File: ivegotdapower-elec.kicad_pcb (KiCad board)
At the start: 2 copper layers, 100 x 50 mm, 0 parts

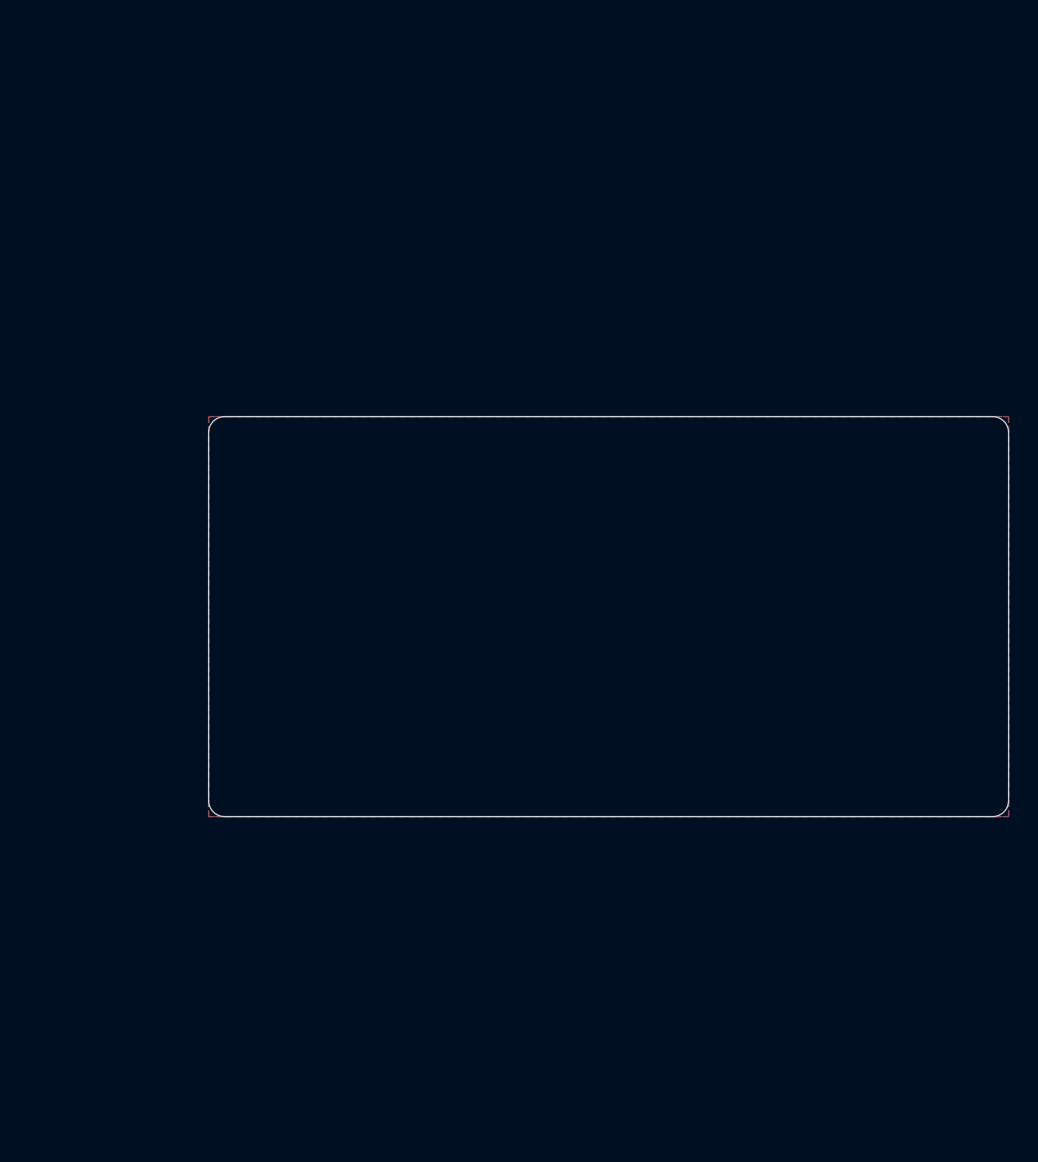
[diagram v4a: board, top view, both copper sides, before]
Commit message: power routed
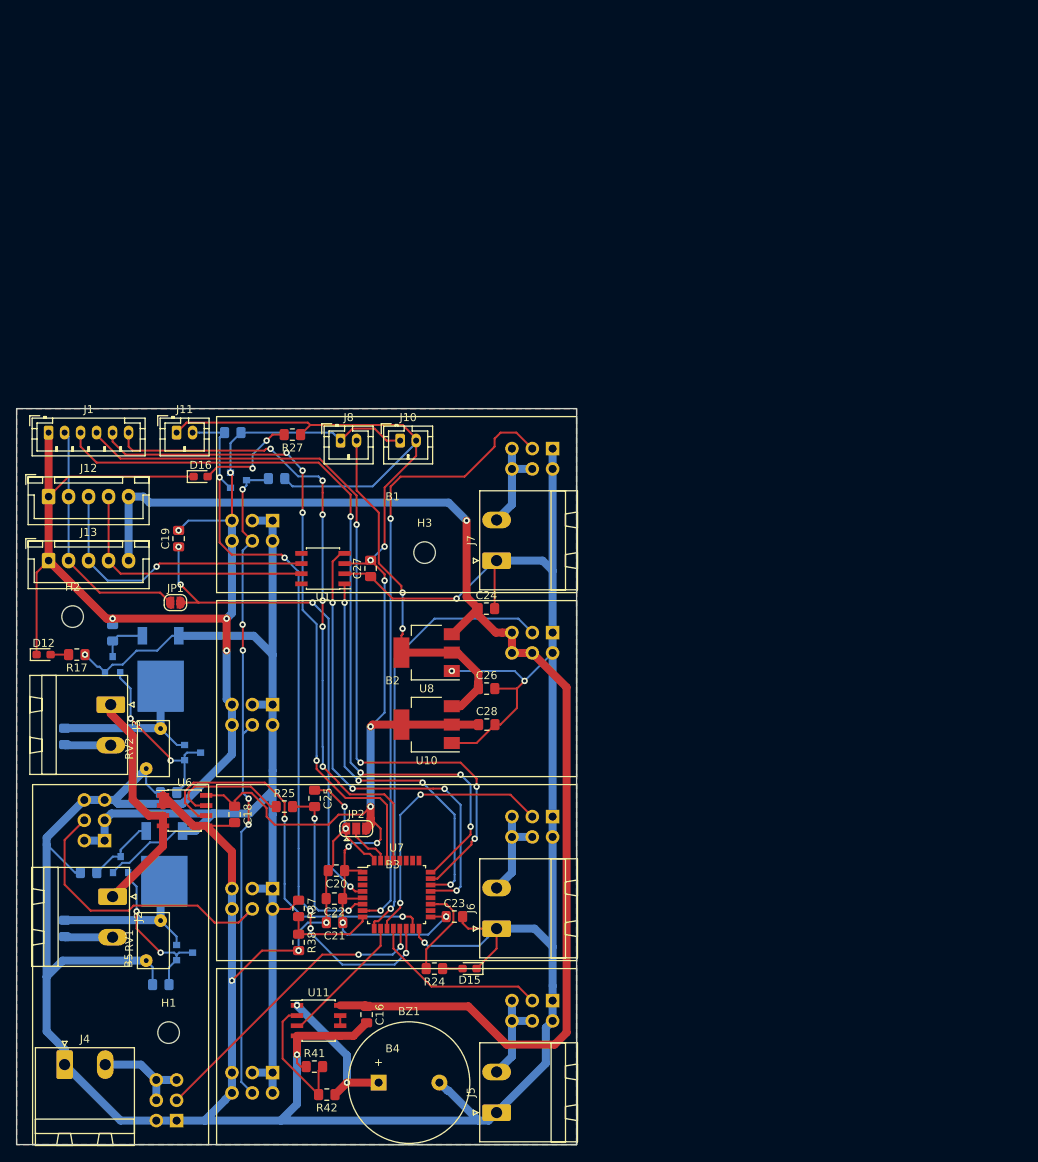
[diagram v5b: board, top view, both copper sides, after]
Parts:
- added B1: board_fille, board_fille:board_fille, F.Cu at (123.0, 110.0)
- added B2: board_fille, board_fille:board_fille, F.Cu at (123.0, 133.0)
- added B3: board_fille, board_fille:board_fille, F.Cu at (123.0, 156.0)
- added B4: board_fille, board_fille:board_fille, F.Cu at (123.0, 179.0)
- added B5: board_fille, board_fille:board_fille, F.Cu at (90.0, 168.0)
- added BZ1: Buzzer, Buzzer_Beeper:Buzzer_15x7.5RM7.6, F.Cu at (121.2, 183.2)
- added C16: C, Capacitor_SMD:C_0805_2012Metric_Pad1.15x1.40mm_HandSolder, F.Cu at (119.8, 174.8)
- added C18: 100nF, Capacitor_SMD:C_0805_2012Metric_Pad1.15x1.40mm_HandSolder, F.Cu at (103.2, 149.7)
- added C19: 100nF, Capacitor_SMD:C_0805_2012Metric_Pad1.15x1.40mm_HandSolder, F.Cu at (96.2, 115.2)
- added C20: 100nF, Capacitor_SMD:C_0805_2012Metric_Pad1.15x1.40mm_HandSolder, F.Cu at (116.0, 156.8)
- added C21: 100nF, Capacitor_SMD:C_0805_2012Metric_Pad1.15x1.40mm_HandSolder, F.Cu at (115.8, 163.2)
- added C22: 4.7uF, Capacitor_SMD:C_0805_2012Metric_Pad1.15x1.40mm_HandSolder, F.Cu at (115.7, 160.2)
- added C23: 100nF, Capacitor_SMD:C_0805_2012Metric_Pad1.15x1.40mm_HandSolder, F.Cu at (130.7, 162.5)
- added C24: 100nF, Capacitor_SMD:C_0805_2012Metric_Pad1.15x1.40mm_HandSolder, F.Cu at (134.7, 124.0)
- added C25: C, Capacitor_SMD:C_0805_2012Metric_Pad1.15x1.40mm_HandSolder, F.Cu at (113.2, 147.7)
- added C26: C, Capacitor_SMD:C_0805_2012Metric_Pad1.15x1.40mm_HandSolder, F.Cu at (134.8, 134.0)
- added C27: 100nF, Capacitor_SMD:C_0805_2012Metric_Pad1.15x1.40mm_HandSolder, F.Cu at (120.2, 119.0)
- added C28: 10uF, Capacitor_SMD:C_0805_2012Metric_Pad1.15x1.40mm_HandSolder, F.Cu at (134.8, 138.5)
- added D12: LED, LED_SMD:LED_0603_1608Metric_Pad1.05x0.95mm_HandSolder, F.Cu at (79.4, 129.8)
- added D15: LED, LED_SMD:LED_0603_1608Metric_Pad1.05x0.95mm_HandSolder, F.Cu at (132.6, 169.0)
- added D16: LED, LED_SMD:LED_0603_1608Metric_Pad1.05x0.95mm_HandSolder, F.Cu at (99.0, 107.5)
- added F6: Fuse, Fuse:Fuse_0805_2012Metric_Pad1.15x1.40mm_HandSolder, B.Cu at (82.0, 164.0)
- added F7: Fuse, Fuse:Fuse_0805_2012Metric_Pad1.15x1.40mm_HandSolder, B.Cu at (82.0, 140.0)
- added H1: MountingHole, MountingHole:MountingHole_2.7mm_M2.5, F.Cu at (95.0, 177.0)
- added H2: MountingHole, MountingHole:MountingHole_2.7mm_M2.5, F.Cu at (83.0, 125.0)
- added H3: MountingHole, MountingHole:MountingHole_2.7mm_M2.5, F.Cu at (127.0, 117.0)
- added J1: Conn_Debug, Connector_JST:JST_PH_B6B-PH-K_1x06_P2.00mm_Vertical, F.Cu at (80.0, 102.0)
- added J10: Conn_+3.3V, Connector_JST:JST_PH_B2B-PH-K_1x02_P2.00mm_Vertical, F.Cu at (123.9, 103.0)
- added J11: Conn_bau, Connector_JST:JST_PH_B2B-PH-K_1x02_P2.00mm_Vertical, F.Cu at (96.0, 102.0)
- added J12: CAN_conn, Connector_JST:JST_XH_B05B-XH-A_1x05_P2.50mm_Vertical, F.Cu at (80.0, 110.0)
- added J13: CAN_conn, Connector_JST:JST_XH_B05B-XH-A_1x05_P2.50mm_Vertical, F.Cu at (80.0, 118.0)
- added J2: Conn_batt, Connector_Phoenix_MSTB:PhoenixContact_MSTBA_2,5_2-G-5,08_1x02_P5.08mm_Horizontal, F.Cu at (88.0, 160.0)
- added J3: Conn_alim, Connector_Phoenix_MSTB:PhoenixContact_MSTBA_2,5_2-G-5,08_1x02_P5.08mm_Horizontal, F.Cu at (87.8, 136.0)
- added J4: Conn_TSMR, Connector_Phoenix_MSTB:PhoenixContact_MSTBA_2,5_2-G-5,08_1x02_P5.08mm_Horizontal, F.Cu at (82.0, 181.0)
- added J5: Conn_POW2, Connector_Phoenix_MSTB:PhoenixContact_MSTBA_2,5_2-G-5,08_1x02_P5.08mm_Horizontal, F.Cu at (136.0, 187.0)
- added J6: Conn_POW1, Connector_Phoenix_MSTB:PhoenixContact_MSTBA_2,5_2-G-5,08_1x02_P5.08mm_Horizontal, F.Cu at (136.0, 164.0)
- added J7: Conn_RPi, Connector_Phoenix_MSTB:PhoenixContact_MSTBA_2,5_2-G-5,08_1x02_P5.08mm_Horizontal, F.Cu at (136.0, 118.0)
- added J8: Conn_+5V, Connector_JST:JST_PH_B2B-PH-K_1x02_P2.00mm_Vertical, F.Cu at (116.5, 103.0)
- added JP1: Jumper_NC_Small, Jumper:SolderJumper-2_P1.3mm_Open_RoundedPad1.0x1.5mm, F.Cu at (95.8, 123.2)
- added JP2: Jumper_NC_Dual, Jumper:SolderJumper-3_P1.3mm_Open_RoundedPad1.0x1.5mm, F.Cu at (118.5, 151.5)
- added Q1: IRFR5305, Package_TO_SOT_SMD:TO-252-2, B.Cu at (94.5, 156.0)
- added Q2: IRFR5305, Package_TO_SOT_SMD:TO-252-2, B.Cu at (94.0, 131.6)
- added Q3: BSS138, Package_TO_SOT_SMD:SOT-23, B.Cu at (103.7, 108.0)
- added Q4: MMBT2907A, Package_TO_SOT_SMD:SOT-23, B.Cu at (97.0, 167.0)
- added Q5: MMBT2907A, Package_TO_SOT_SMD:SOT-23, B.Cu at (98.0, 142.0)
- added Q6: MMBT2907A, Package_TO_SOT_SMD:SOT-23, B.Cu at (89.0, 156.0)
- added Q7: MMBT2907A, Package_TO_SOT_SMD:SOT-23, B.Cu at (88.0, 131.0)
- added R16: 1k, Resistor_SMD:R_0805_2012Metric_Pad1.15x1.40mm_HandSolder, B.Cu at (103.0, 102.0)
- added R17: R, Resistor_SMD:R_0805_2012Metric_Pad1.15x1.40mm_HandSolder, F.Cu at (83.5, 129.8)
- added R24: R, Resistor_SMD:R_0805_2012Metric_Pad1.15x1.40mm_HandSolder, F.Cu at (128.2, 169.0)
- added R25: R, Resistor_SMD:R_0805_2012Metric_Pad1.15x1.40mm_HandSolder, F.Cu at (109.5, 148.8)
- added R27: R, Resistor_SMD:R_0805_2012Metric_Pad1.15x1.40mm_HandSolder, F.Cu at (110.5, 102.2)
- added R30: R, Resistor_SMD:R_0805_2012Metric_Pad1.15x1.40mm_HandSolder, B.Cu at (108.5, 107.8)
- added R33: R, Resistor_SMD:R_0805_2012Metric_Pad1.15x1.40mm_HandSolder, B.Cu at (94.0, 171.0)
- added R34: R, Resistor_SMD:R_0805_2012Metric_Pad1.15x1.40mm_HandSolder, B.Cu at (95.0, 147.0)
- added R35: R, Resistor_SMD:R_0805_2012Metric_Pad1.15x1.40mm_HandSolder, B.Cu at (85.0, 157.0)
- added R36: R, Resistor_SMD:R_0805_2012Metric_Pad1.15x1.40mm_HandSolder, B.Cu at (88.0, 127.0)
- added R37: R, Resistor_SMD:R_0805_2012Metric_Pad1.15x1.40mm_HandSolder, F.Cu at (111.2, 161.5)
- added R38: R, Resistor_SMD:R_0805_2012Metric_Pad1.15x1.40mm_HandSolder, F.Cu at (111.2, 165.7)
- added R41: R, Resistor_SMD:R_0805_2012Metric_Pad1.15x1.40mm_HandSolder, F.Cu at (113.2, 181.2)
- added R42: R, Resistor_SMD:R_0805_2012Metric_Pad1.15x1.40mm_HandSolder, F.Cu at (114.8, 184.8)
- added RV1: Varistor, Varistor:RV_Disc_D7mm_W4mm_P5mm, F.Cu at (94.0, 163.0)
- added RV2: Varistor, Varistor:RV_Disc_D7mm_W4mm_P5mm, F.Cu at (94.0, 139.0)
- added U1: TCAN332, Package_SO:SOIC-8_3.9x4.9mm_P1.27mm, F.Cu at (114.3, 119.0)
- added U10: LD1117S33TR_SOT223, Package_TO_SOT_SMD:SOT-223-3_TabPin2, F.Cu at (127.2, 138.5)
- added U11: LM358, Package_SO:SOIC-8_3.9x4.9mm_P1.27mm, F.Cu at (113.8, 175.5)
- added U6: ACS711xLCTR-12AB, Package_SO:SOIC-8_3.9x4.9mm_P1.27mm, F.Cu at (97.0, 149.2)
- added U7: STM32F303K8Tx, Package_QFP:LQFP-32_7x7mm_P0.8mm, F.Cu at (123.5, 159.8)
- added U8: LD1117S50TR_SOT223, Package_TO_SOT_SMD:SOT-223-3_TabPin2, F.Cu at (127.2, 129.5)
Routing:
- net GND: track 0.00 -> 599.6 mm, vias 0 -> 15
- net +3V3: track 0.00 -> 186.8 mm, vias 0 -> 9
- net +7.5V: track 0.00 -> 158.9 mm, vias 0 -> 1
- net /buck/power: track 0.00 -> 156.1 mm, vias 0 -> 1
- net /buck/on-off: track 0.00 -> 121.2 mm, vias 0 -> 5
- net /STM32/TCK: track 0.00 -> 100.8 mm, vias 0 -> 4
- net /STM32/TMS: track 0.00 -> 100.2 mm, vias 0 -> 4
- net /buck/bau: track 0.00 -> 94.3 mm, vias 0 -> 5
- net /STM32/RX_1: track 0.00 -> 82.3 mm, vias 0 -> 4
- net /STM32/TX_1: track 0.00 -> 81.8 mm, vias 0 -> 6
- net /buck/RPi_mes: track 0.00 -> 77.7 mm, vias 0 -> 2
- net Net-(C19-Pad1): track 0.00 -> 63.7 mm, vias 0 -> 4
- net /STM32/CAN_RX: track 0.00 -> 59.9 mm, vias 0 -> 4
- net /buck/Logic_mes: track 0.00 -> 55.1 mm, vias 0 -> 1
- net /STM32/CAN_TX: track 0.00 -> 50.6 mm, vias 0 -> 4
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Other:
- board size 100 x 50 mm -> 70 x 92 mm
- net class Power_fat added: clearance 0.5, trace_width 2, via_dia 0.8, via_drill 0.4

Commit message: update board_fille
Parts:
- moved B1 23.9 mm to (101.0, 100.6)
- moved B2 23.9 mm to (101.0, 123.6)
- moved B3 23.9 mm to (101.0, 146.6)
- moved B4 23.9 mm to (101.0, 169.6)
- moved B5 23.9 mm to (99.4, 146.0)

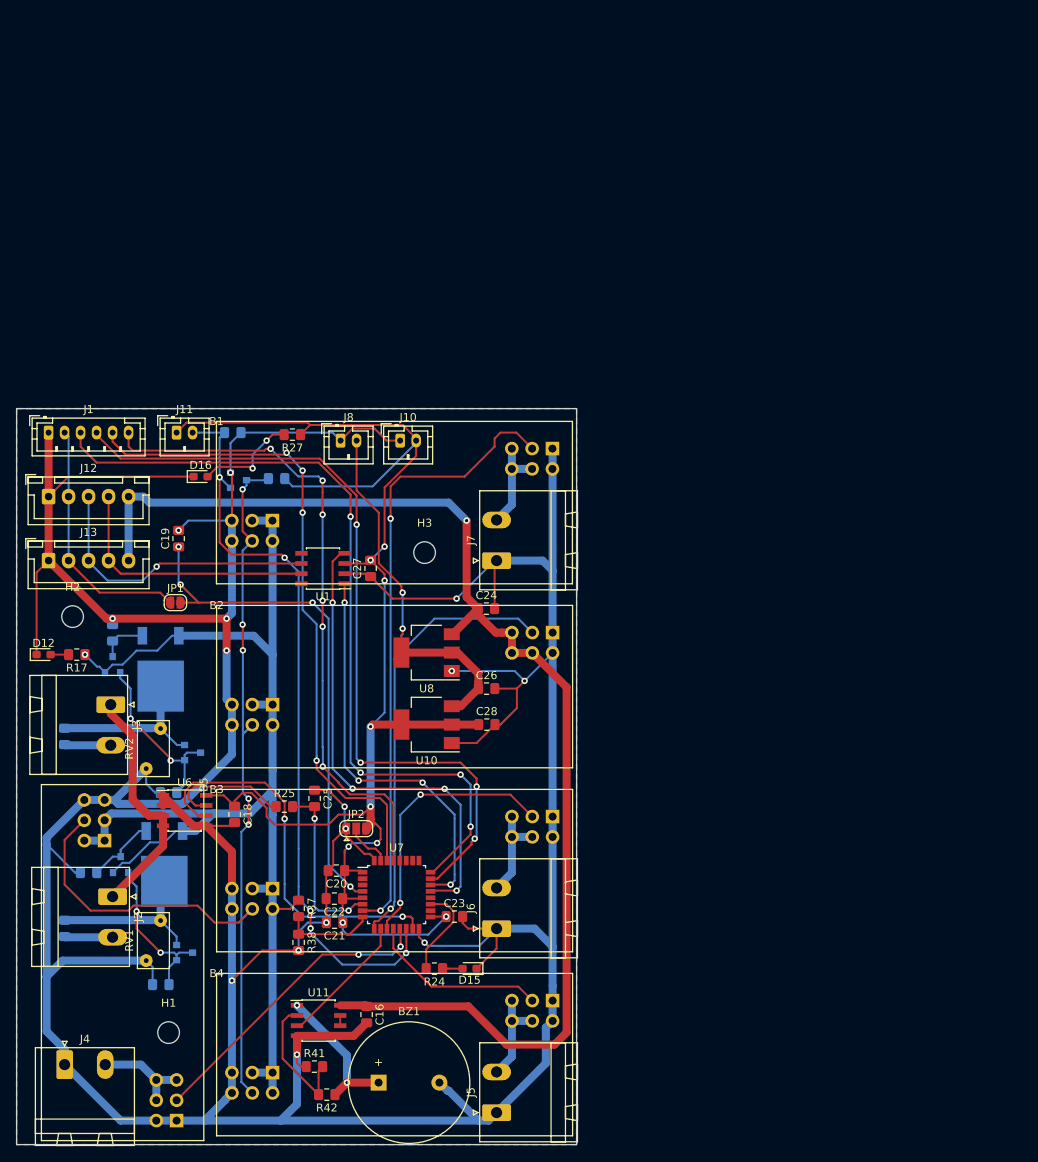
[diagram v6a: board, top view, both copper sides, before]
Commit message: Placement and routing done
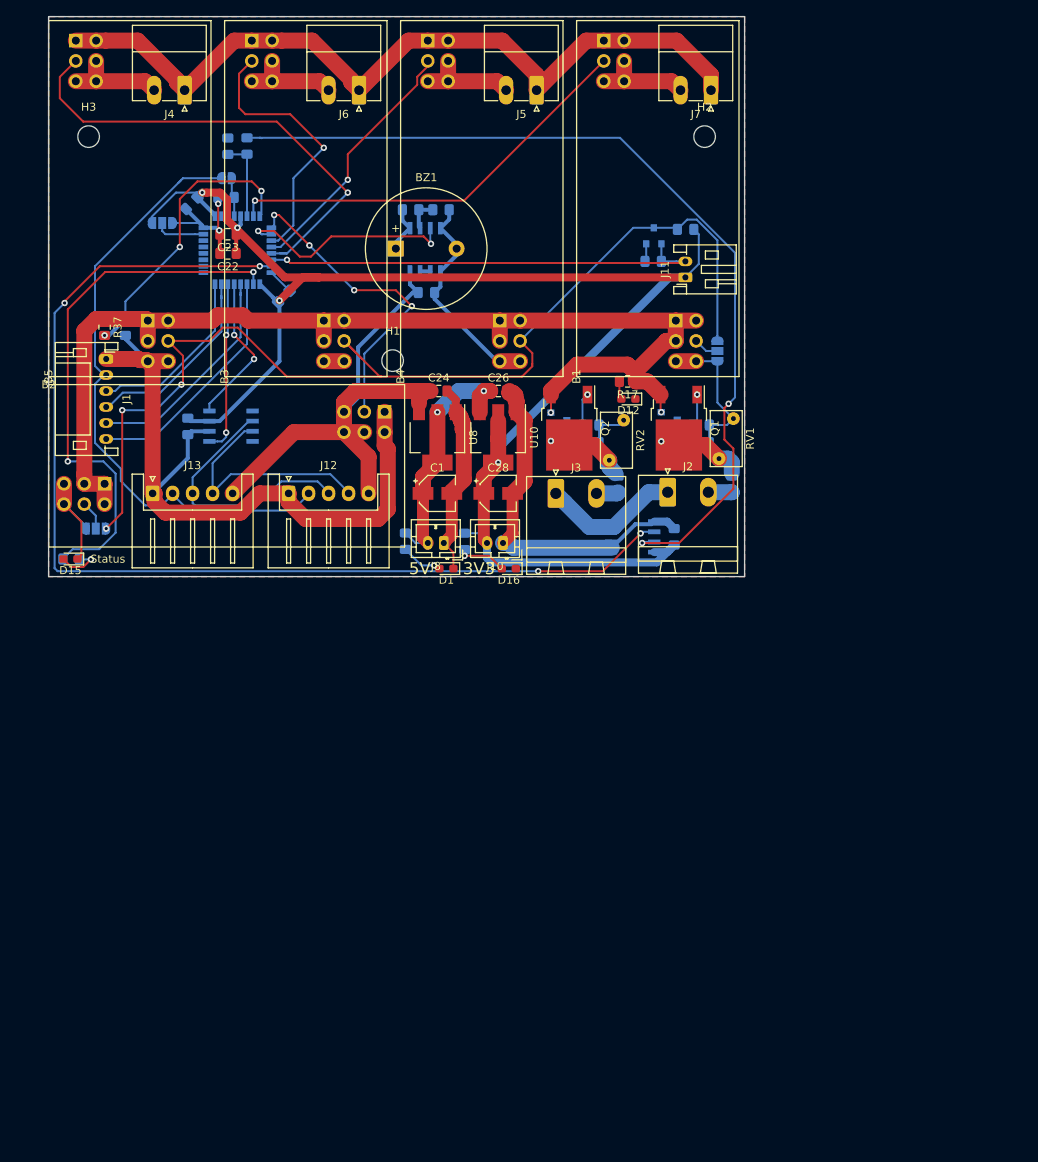
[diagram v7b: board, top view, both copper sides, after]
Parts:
- added C1: 10uF, Capacitor_SMD:CP_Elec_4x5.4, F.Cu at (128.6, 109.6)
- added D1: LED, LED_SMD:LED_0603_1608Metric_Pad1.05x0.95mm_HandSolder, F.Cu at (129.7, 119.0)
- added JP3: Jumper_NC_Dual, Jumper:SolderJumper-3_P1.3mm_Open_RoundedPad1.0x1.5mm, B.Cu at (163.6, 91.8)
- added JP4: Jumper_NC_Dual, Jumper:SolderJumper-3_P1.3mm_Open_RoundedPad1.0x1.5mm, B.Cu at (85.9, 114.0)
- added R1: R, Resistor_SMD:R_0805_2012Metric_Pad1.15x1.40mm_HandSolder, B.Cu at (124.6, 115.6)
- C16, C18, C19, C20, C21, C25, C27, JP1, JP2, R24, R25, R27, R38, R41, R42, U1, U11, U6, U7: moved to B.Cu
- C28: footprint Capacitor_SMD:C_0805_2012Metric_Pad1.15x1.40mm_HandSolder -> Capacitor_SMD:CP_Elec_4x5.4
- J1: footprint Connector_JST:JST_PH_B6B-PH-K_1x06_P2.00mm_Vertical -> Connector_JST:JST_PH_S6B-PH-K_1x06_P2.00mm_Horizontal
- J11: footprint Connector_JST:JST_PH_B2B-PH-K_1x02_P2.00mm_Vertical -> Connector_JST:JST_PH_S2B-PH-K_1x02_P2.00mm_Horizontal
- J12, J13: footprint Connector_JST:JST_XH_B05B-XH-A_1x05_P2.50mm_Vertical -> Connector_JST:JST_XH_S05B-XH-A_1x05_P2.50mm_Horizontal
- J4, J5, J6, J7: footprint Connector_Phoenix_MSTB:PhoenixContact_MSTBA_2,5_2-G-5,08_1x02_P5.08mm_Horizontal -> Connector_Phoenix_MC:PhoenixContact_MC_1,5_2-G-3.81_1x02_P3.81mm_Horizontal
- Q1, Q2: moved to F.Cu
- moved J5 127.9 mm to (141.0, 59.2), turned to 180 degrees
- moved J4 122.7 mm to (97.0, 59.2), turned to 180 degrees
- moved R42 111.1 mm to (125.3, 74.1), turned to 0 degrees
- moved R41 108.3 mm to (129.1, 74.1), turned to 180 degrees
- moved J6 106.2 mm to (118.8, 59.2), turned to 180 degrees
- moved BZ1 104.3 mm to (123.4, 79.0)
- moved F6 100.2 mm to (165.4, 108.5)
- moved H2 99.2 mm to (162.0, 65.0)
- moved U11 97.3 mm to (127.1, 79.1), turned to 270 degrees
- moved R33 95.7 mm to (161.6, 103.3), turned to 0 degrees
- moved R35 94.8 mm to (161.6, 101.1), turned to 0 degrees
- moved RV1 90.6 mm to (163.8, 105.3), turned to 90 degrees
- moved C16 90.6 mm to (127.2, 84.5), turned to 0 degrees
- moved C23 89.9 mm to (102.4, 77.2), turned to 180 degrees
- moved H1 88.5 mm to (123.0, 93.0)
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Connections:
- B1 pad 4: /buck/on-off -> Net-(B1-Pad4)
- B2 pad 4: /buck/on-off -> Net-(B2-Pad4)
- U1 pad 5: Net-(U1-Pad5) -> (no net)
- U1 pad 8: Net-(U1-Pad8) -> (no net)
- U7 pad 18: Net-(U7-Pad18) -> Net-(R24-Pad2)
- U7 pad 19: Net-(R24-Pad2) -> /STM32/TX_1
- U7 pad 2: Net-(U7-Pad2) -> (no net)
- U7 pad 20: Net-(U7-Pad20) -> /STM32/RX_1
- U7 pad 25: Net-(U7-Pad25) -> (no net)
- U7 pad 26: Net-(U7-Pad26) -> (no net)
- U7 pad 27: Net-(U7-Pad27) -> (no net)
- U7 pad 28: Net-(U7-Pad28) -> (no net)
- U7 pad 29: /STM32/TX_1 -> (no net)
- U7 pad 3: Net-(U7-Pad3) -> (no net)
- U7 pad 30: /STM32/RX_1 -> (no net)
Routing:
- net GND: track 599.6 -> 351.0 mm, vias 15 -> 2
- net /STM32/sense: track 15.6 -> 113.4 mm, vias 0 -> 2
- net /STM32/sense_fault: track 49.0 -> 138.7 mm, vias 2 -> 4
- net +7.5V: track 158.9 -> 71.1 mm, vias 1 -> 0
- net /STM32/TCK: track 100.8 -> 22.8 mm, vias 4 -> 0
- net /STM32/TMS: track 100.2 -> 24.5 mm, vias 4 -> 0
- net Net-(C19-Pad1): track 63.7 -> 4.87 mm, vias 4 -> 0
- net Net-(R24-Pad2): track 11.8 -> 67.6 mm, vias 0 -> 2
- net /STM32/RX_1: track 82.3 -> 28.2 mm, vias 4 -> 0
- net /STM32/TX_1: track 81.8 -> 30.0 mm, vias 6 -> 0
- net /STM32/nrst: track 31.2 -> 77.5 mm
- net /STM32/CAN_RX: track 59.9 -> 19.2 mm, vias 4 -> 2
- net /buck/bau: track 94.3 -> 57.2 mm, vias 5 -> 1
- net +3V3: track 186.8 -> 217.5 mm, vias 9 -> 4
- net /STM32/CAN_TX: track 50.6 -> 21.5 mm, vias 4 -> 2
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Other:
- board size 70 x 92 mm -> 87 x 70 mm
- board text added: "3V3"
- board text added: "5V"
- board text added: "Status"
